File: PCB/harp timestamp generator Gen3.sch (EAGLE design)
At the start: 140 parts, among them IC1 MCP73831T-2ATI/OT, IC10 SN74LVC1G125DBVT, IC11 TLV70033DDCR, IC12 SI8621BC-B-IS, IC13 SI8621BC-B-IS, IC14 SI8621BC-B-IS, IC15 SI8621BC-B-IS, IC16 SI8621BC-B-IS, IC17 SI8621BC-B-IS, IC18 SN74LVC1G125DBVT, IC19 SN74LVC1G125DBVT, IC2 USBLC6-2SC6, IC3 FT232RL, IC4 ICL7673CBAZA-T, IC5 TLV70033DDCR, IC6 ATXMEGA16A4U-AU, IC7 M74VHC1GT126DF1G, IC8 M74VHC1GT126DF1G, IC9 M74VHC1GT126DF1G, Q1 RTU002P02T106, Q2 BC817-40W, Q3 BC817-40LT1SMD, Q4 DMG1012UW, Q5 DMP2035U-7, T1 BC850, T10 BC850, T2 BC850, T3 BC850, T4 BC850, T5 BC850, T6 BC850, T7 BC850, T8 BC850, T9 BC850, X1 B2B-PH-K-S(LF)(SN)

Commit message: Added an extra 100uF capacitor to +5_USB.
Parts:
- added C39: 100u 25V, rcl:CPOL-EUTT2D6
- C8: device rcl:CPOL-EUA/3216-18W -> rcl:C-EUC0603; DIGKEYPN 478-11183-1-ND -> 587-2786-1-ND; MPN TAJA475K010TNJ -> EMK107ABJ475KA-T
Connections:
- net +5_USB: now also C39.+, C8.1; no longer C8.+
- net GND: now also C39.-, C8.2; no longer C8.-
- net LED_CLK_1: now also IC6.PA7/ADC7/AC0-OUT, R22.1; no longer IC6.PC1/OC0B/XCK0/SCL, R27.1
- net LED_CLK_2: now also IC6.PC4/OC1A/#SS, R23.1; no longer IC6.PC2/OC0C/RXD0, R22.1
- net LED_CLK_3: now also IC6.PC1/OC0B/XCK0/SCL, R27.1; no longer IC6.PC3/OC0D/TXD0, R28.1
- net LED_CLK_4: now also IC6.PA6/ADC6, R28.1; no longer IC6.PC4/OC1A/#SS, R23.1
- net UC_RX: now also IC6.PC2/OC0C/RXD0; no longer IC6.PA6/ADC6
- net UC_TX: now also IC6.PC3/OC0D/TXD0; no longer IC6.PA7/ADC7/AC0-OUT
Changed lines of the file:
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@@
 <attribute name="MPN" value="CGA2B3X7R1H104K050BB"/>
 </part>
-<part name="C8" library="rcl" deviceset="CPOL-EU" device="A/3216-18W" value="4.7uF">
-<attribute name="DIGKEYPN" value="478-11183-1-ND"/>
-<attribute name="MPN" value="TAJA475K010TNJ"/>
-</part>
 <part name="C9" library="rcl" deviceset="C-EU" device="C0402" value="100nF">
 <attribute name="DIGKEYPN" value="445-6899-2-ND"/>
@@
 <attribute name="DIGKEYPN" value=""/>
 </part>
+<part name="C39" library="rcl" library_urn="urn:adsk.eagle:library:334" deviceset="CPOL-EU" device="TT2D6" package3d_urn="urn:adsk.eagle:package:23303/1" value="100u 25V">
+<attribute name="MPN" value="EEUFM1E101B"/>
+<attribute name="NOTES" value="-"/>
+<attribute name="TYPE" value="TH"/>
+</part>
+<part name="GND72" library="supply1" deviceset="GND" device="">
+<attribute name="DIGKEYPN" value=""/>
+<attribute name="MPN" value=""/>
+</part>
+<part name="C8" library="rcl" deviceset="C-EU" device="C0603" value="4.7uF">
+<attribute name="DIGKEYPN" value="587-2786-1-ND"/>
+<attribute name="MPN" value="EMK107ABJ475KA-T"/>
+</part>
 </parts>
 <sheets>
@@
 <attribute name="DIGKEYPN" x="137.16" y="391.16" size="1.778" layer="96" rot="MR0" display="off"/>
 </instance>
-<instance part="C8" gate="G$1" x="147.32" y="391.16" smashed="yes" rot="MR0">
-<attribute name="NAME" x="146.177" y="391.6426" size="1.778" layer="95" rot="MR0"/>
-<attribute name="VALUE" x="146.177" y="386.5626" size="1.778" layer="96" rot="MR0"/>
-<attribute name="MPN" x="147.32" y="391.16" size="1.778" layer="96" rot="MR0" display="off"/>
-<attribute name="MPN" x="147.32" y="391.16" size="1.778" layer="96" rot="MR0" display="off"/>
-<attribute name="MPN" x="147.32" y="391.16" size="1.778" layer="96" rot="MR0" display="off"/>
-<attribute name="DIGKEYPN" x="147.32" y="391.16" size="1.778" layer="96" rot="MR0" display="off"/>
-</instance>
 <instance part="C9" gate="G$1" x="157.48" y="391.16" smashed="yes" rot="MR0">
 <attribute name="NAME" x="155.956" y="391.541" size="1.778" layer="95" rot="MR0"/>
@@
 <attribute name="DIGKEYPN" x="467.36" y="391.16" size="1.778" layer="96" rot="MR0" display="off"/>
 </instance>
+<instance part="C39" gate="G$1" x="109.22" y="391.16" smashed="yes">
+<attribute name="NAME" x="102.743" y="391.6426" size="1.778" layer="95"/>
+<attribute name="VALUE" x="96.393" y="386.3086" size="1.778" layer="96"/>
+<attribute name="MPN" x="109.22" y="391.16" size="1.778" layer="96" display="off"/>
+<attribute name="TYPE" x="109.22" y="391.16" size="1.778" layer="96" display="off"/>
+<attribute name="TYPE" x="109.22" y="391.16" size="1.778" layer="96" display="off"/>
+<attribute name="TYPE" x="109.22" y="391.16" size="1.778" layer="96" display="off"/>
+<attribute name="TYPE" x="109.22" y="391.16" size="1.778" layer="96" display="off"/>
+<attribute name="TYPE" x="109.22" y="391.16" size="1.778" layer="96" display="off"/>
+<attribute name="TYPE" x="109.22" y="391.16" size="1.778" layer="96" display="off"/>
+<attribute name="TYPE" x="109.22" y="391.16" size="1.778" layer="96" display="off"/>
+<attribute name="TYPE" x="109.22" y="391.16" size="1.778" layer="96" display="off"/>
+<attribute name="TYPE" x="109.22" y="391.16" size="1.778" layer="96" display="off"/>
+<attribute name="TYPE" x="109.22" y="391.16" size="1.778" layer="96" display="off"/>
+<attribute name="TYPE" x="109.22" y="391.16" size="1.778" layer="96" display="off"/>
+<attribute name="TYPE" x="109.22" y="391.16" size="1.778" layer="96" display="off"/>
+<attribute name="TYPE" x="109.22" y="391.16" size="1.778" layer="96" display="off"/>
+<attribute name="NOTES" x="109.22" y="391.16" size="1.778" layer="96" display="off"/>
+<attribute name="NOTES" x="109.22" y="391.16" size="1.778" layer="96" display="off"/>
+<attribute name="NOTES" x="109.22" y="391.16" size="1.778" layer="96" display="off"/>
+<attribute name="NOTES" x="109.22" y="391.16" size="1.778" layer="96" display="off"/>
+<attribute name="NOTES" x="109.22" y="391.16" size="1.778" layer="96" display="off"/>
+<attribute name="NOTES" x="109.22" y="391.16" size="1.778" layer="96" display="off"/>
+<attribute name="NOTES" x="109.22" y="391.16" size="1.778" layer="96" display="off"/>
+<attribute name="NOTES" x="109.22" y="391.16" size="1.778" layer="96" display="off"/>
+<attribute name="NOTES" x="109.22" y="391.16" size="1.778" layer="96" display="off"/>
+<attribute name="NOTES" x="109.22" y="391.16" size="1.778" layer="96" display="off"/>
+<attribute name="NOTES" x="109.22" y="391.16" size="1.778" layer="96" display="off"/>
+</instance>
+<instance part="GND72" gate="1" x="109.22" y="381" smashed="yes" rot="MR0">
+<attribute name="VALUE" x="111.76" y="378.46" size="1.778" layer="96" rot="MR0"/>
+<attribute name="MPN" x="109.22" y="381" size="1.778" layer="96" rot="MR0" display="off"/>
+<attribute name="MPN" x="109.22" y="381" size="1.778" layer="96" rot="MR0" display="off"/>
+<attribute name="DIGKEYPN" x="109.22" y="381" size="1.778" layer="96" rot="MR0" display="off"/>
+</instance>
+<instance part="C8" gate="G$1" x="147.32" y="391.16" smashed="yes" rot="MR0">
+<attribute name="NAME" x="145.796" y="391.541" size="1.778" layer="95" rot="MR0"/>
+<attribute name="VALUE" x="145.796" y="386.461" size="1.778" layer="96" rot="MR0"/>
+<attribute name="MPN" x="147.32" y="391.16" size="1.778" layer="96" rot="MR0" display="off"/>
+<attribute name="MPN" x="147.32" y="391.16" size="1.778" layer="96" rot="MR0" display="off"/>
+<attribute name="DIGKEYPN" x="147.32" y="391.16" size="1.778" layer="96" rot="MR0" display="off"/>
+</instance>
 </instances>
 <busses>
@@
 </segment>
 <segment>
-<pinref part="C8" gate="G$1" pin="-"/>
 <wire x1="147.32" y1="386.08" x2="147.32" y2="383.54" width="0.1524" layer="91"/>
 <pinref part="GND43" gate="1" pin="GND"/>
+<pinref part="C8" gate="G$1" pin="2"/>
 </segment>
 <segment>
@@
 <wire x1="408.94" y1="439.42" x2="408.94" y2="444.5" width="0.1524" layer="91"/>
 </segment>
+<segment>
+<pinref part="C39" gate="G$1" pin="-"/>
+<pinref part="GND72" gate="1" pin="GND"/>
+<wire x1="109.22" y1="386.08" x2="109.22" y2="383.54" width="0.1524" layer="91"/>
+</segment>
 </net>
 <net name="CLOCK_IN" class="0">
@@
 <pinref part="L1" gate="G$1" pin="1"/>
 <wire x1="165.1" y1="398.78" x2="147.32" y2="398.78" width="0.1524" layer="91"/>
-<pinref part="C8" gate="G$1" pin="+"/>
 <wire x1="147.32" y1="398.78" x2="137.16" y2="398.78" width="0.1524" layer="91"/>
 <wire x1="147.32" y1="393.7" x2="147.32" y2="398.78" width="0.1524" layer="91"/>
@@
 <pinref part="Q5" gate="G$1" pin="S"/>
 <label x="124.46" y="398.78" size="1.778" layer="95"/>
+<pinref part="C39" gate="G$1" pin="+"/>
+<wire x1="119.38" y1="398.78" x2="109.22" y2="398.78" width="0.1524" layer="91"/>
+<wire x1="109.22" y1="398.78" x2="109.22" y2="393.7" width="0.1524" layer="91"/>
+<pinref part="C8" gate="G$1" pin="1"/>
 </segment>
 </net>
@@
 </segment>
 </net>
-<net name="LED_CLK_1" class="0">
+<net name="LED_CLK_3" class="0">
 <segment>
 <pinref part="IC6" gate="G$1" pin="PC1/OC0B/XCK0/SCL"/>
@@
 </segment>
 </net>
-<net name="LED_CLK_2" class="0">
-<segment>
-<pinref part="IC6" gate="G$1" pin="PC2/OC0C/RXD0"/>
-<wire x1="609.6" y1="444.5" x2="589.28" y2="444.5" width="0.1524" layer="91"/>
-<label x="589.28" y="444.5" size="1.778" layer="95"/>
-</segment>
+<net name="LED_CLK_1" class="0">
 <segment>
 <pinref part="R22" gate="G$1" pin="1"/>
@@
 <label x="541.02" y="147.32" size="1.778" layer="95"/>
 </segment>
-</net>
-<net name="LED_CLK_3" class="0">
 <segment>
-<pinref part="IC6" gate="G$1" pin="PC3/OC0D/TXD0"/>
-<wire x1="609.6" y1="441.96" x2="589.28" y2="441.96" width="0.1524" layer="91"/>
-<label x="589.28" y="441.96" size="1.778" layer="95"/>
+<wire x1="609.6" y1="469.9" x2="589.28" y2="469.9" width="0.1524" layer="91"/>
+<label x="589.28" y="469.9" size="1.778" layer="95"/>
+<pinref part="IC6" gate="G$1" pin="PA7/ADC7/AC0-OUT"/>
 </segment>
+</net>
+<net name="LED_CLK_4" class="0">
 <segment>
 <pinref part="R28" gate="G$1" pin="1"/>
@@
 <label x="541.02" y="99.06" size="1.778" layer="95"/>
 </segment>
+<segment>
+<wire x1="609.6" y1="472.44" x2="589.28" y2="472.44" width="0.1524" layer="91"/>
+<label x="589.28" y="472.44" size="1.778" layer="95"/>
+<pinref part="IC6" gate="G$1" pin="PA6/ADC6"/>
+</segment>
 </net>
-<net name="LED_CLK_4" class="0">
+<net name="LED_CLK_2" class="0">
 <segment>
 <pinref part="IC6" gate="G$1" pin="PC4/OC1A/#SS"/>
@@
 <net name="UC_RX" class="0">
 <segment>
-<wire x1="609.6" y1="472.44" x2="589.28" y2="472.44" width="0.1524" layer="91"/>
-<label x="589.28" y="472.44" size="1.778" layer="95"/>
-<pinref part="IC6" gate="G$1" pin="PA6/ADC6"/>
-</segment>
-<segment>
 <wire x1="589.28" y1="309.88" x2="624.84" y2="309.88" width="0.1524" layer="91"/>
 <label x="624.84" y="309.88" size="1.778" layer="95" rot="MR0"/>
 <pinref part="IC10" gate="A" pin="O"/>
 </segment>
-</net>
-<net name="UC_TX" class="0">
 <segment>
-<wire x1="609.6" y1="469.9" x2="589.28" y2="469.9" width="0.1524" layer="91"/>
-<label x="589.28" y="469.9" size="1.778" layer="95"/>
-<pinref part="IC6" gate="G$1" pin="PA7/ADC7/AC0-OUT"/>
+<pinref part="IC6" gate="G$1" pin="PC2/OC0C/RXD0"/>
+<wire x1="609.6" y1="444.5" x2="589.28" y2="444.5" width="0.1524" layer="91"/>
+<label x="589.28" y="444.5" size="1.778" layer="95"/>
 </segment>
+</net>
+<net name="UC_TX" class="0">
 <segment>
 <pinref part="IC9" gate="A" pin="I"/>
@@
 <label x="508" y="309.88" size="1.778" layer="95" rot="MR0"/>
 </segment>
+<segment>
+<pinref part="IC6" gate="G$1" pin="PC3/OC0D/TXD0"/>
+<wire x1="609.6" y1="441.96" x2="589.28" y2="441.96" width="0.1524" layer="91"/>
+<label x="589.28" y="441.96" size="1.778" layer="95"/>
+</segment>
 </net>

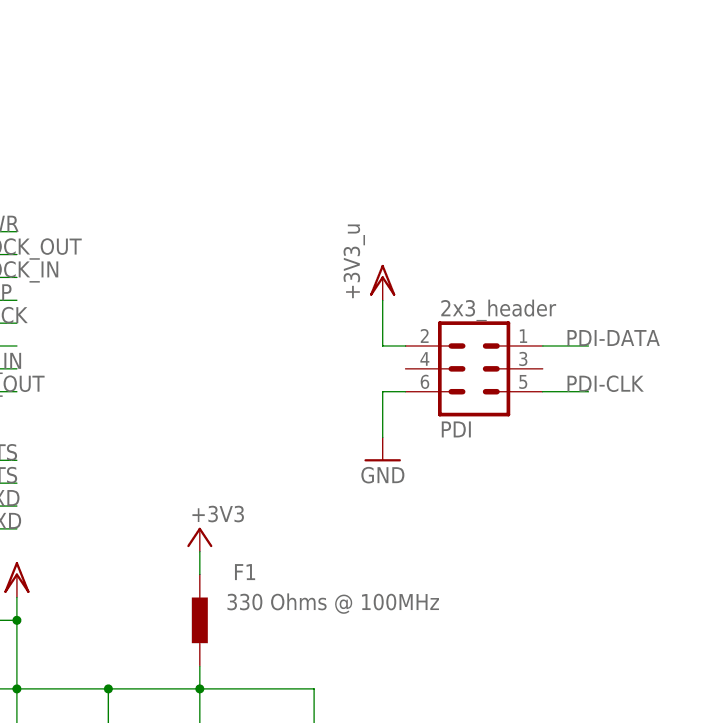
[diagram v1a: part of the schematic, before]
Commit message: Added proper filtering to RESET line.
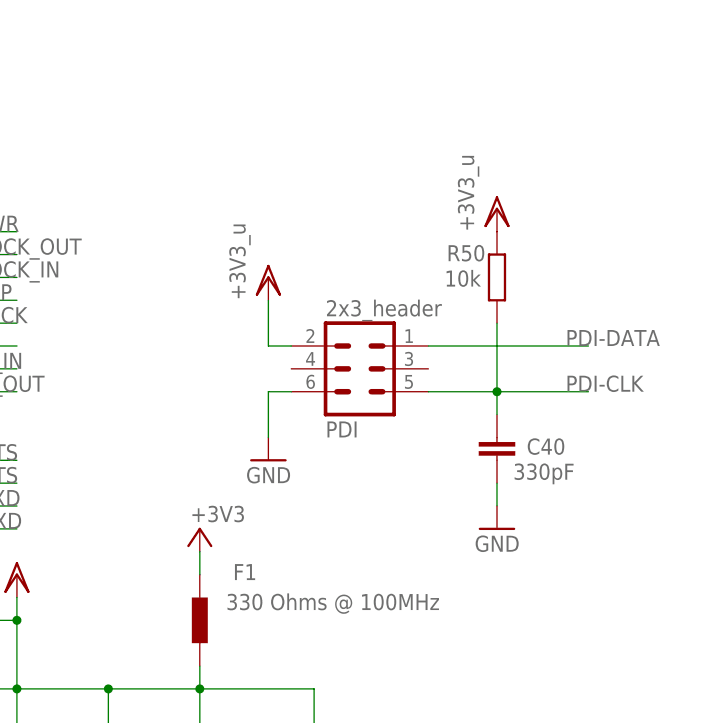
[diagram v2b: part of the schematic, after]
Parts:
- added C40: 330pF, rcl:C-EUC0402
- added R50: 10k, rcl:R-EU_R0402
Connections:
- net GND: now also C40.2
- net PDI-CLK: now also C40.1, R50.1
- net VDD: now also R50.2
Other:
- moved on the sheet: PDI

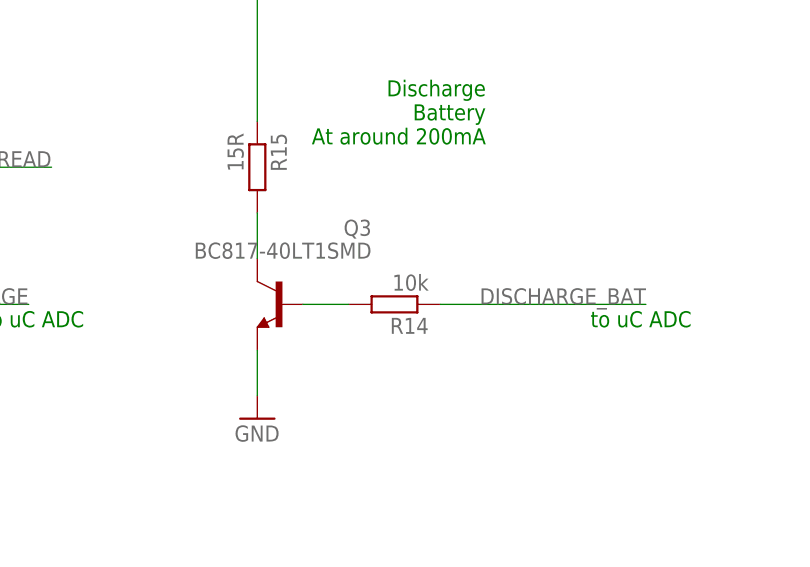
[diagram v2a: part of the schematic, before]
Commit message: Corrected the discharge circuit.
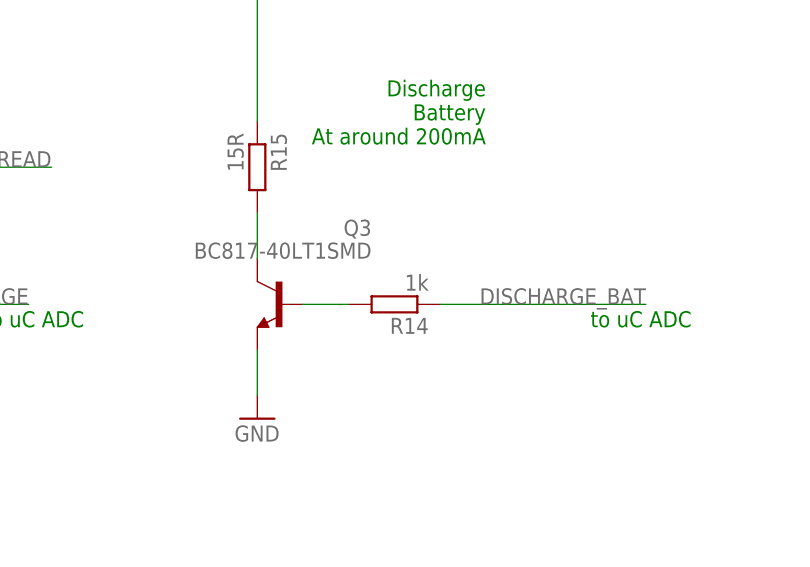
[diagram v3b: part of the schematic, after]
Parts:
- R14: value 10k -> 1k
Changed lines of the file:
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@@
 <attribute name="MPN" value="SBC817-40LT1G"/>
 </part>
-<part name="R14" library="rcl" deviceset="R-EU_" device="R0402" value="10k">
+<part name="R14" library="rcl" deviceset="R-EU_" device="R0402" value="1k">
 <attribute name="DIGKEYPN" value="541-3959-1-ND"/>
 <attribute name="MPN" value="CRCW040210K0FKEDC"/>
